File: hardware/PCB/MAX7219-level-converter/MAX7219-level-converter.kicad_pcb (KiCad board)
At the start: 2 copper layers, 21.5 x 10 mm, 4 parts, among them U1 SN74LV1T34DBV, U2 MAX7219, U3 SN74LV1T34DBV, U4 SN74LV1T34DBV

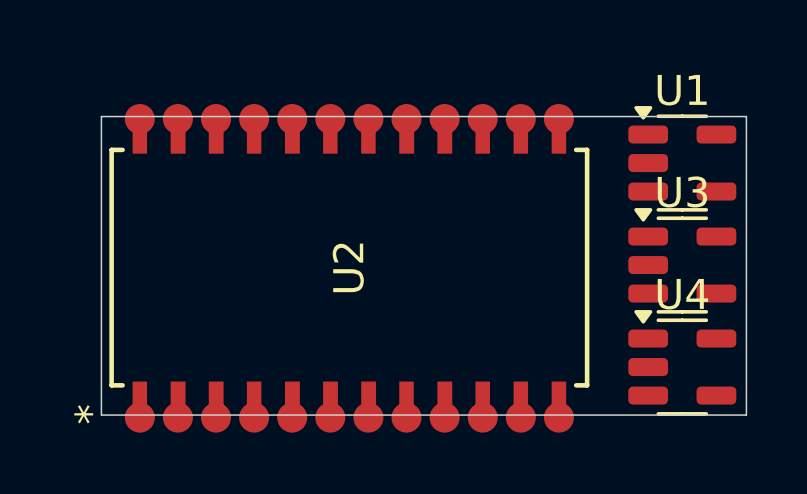
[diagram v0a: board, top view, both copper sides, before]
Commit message: signal level converter for new hardware version 1.0
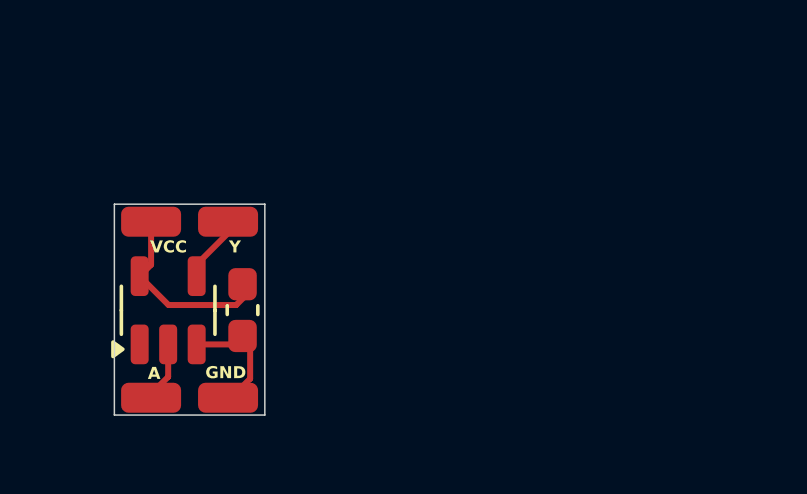
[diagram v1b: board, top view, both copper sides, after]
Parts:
- removed U2: MAX7219, MAX7219:MAX7219-pigipack
- removed U3, U4: SN74LV1T34DBV, Package_TO_SOT_SMD:SOT-23-5
- added C1: 100n/50V, Capacitor_SMD:C_0603_1608Metric_Pad1.08x0.95mm_HandSolder, F.Cu at (140.0, 98.6)
- added J1: VCC, Connector_Wire:SolderWirePad_1x01_SMD_1x2mm, F.Cu at (136.9, 95.6)
- added J2: GND, Connector_Wire:SolderWirePad_1x01_SMD_1x2mm, F.Cu at (139.5, 101.5)
- added J3: Conn_01x01_Pin, Connector_Wire:SolderWirePad_1x01_SMD_1x2mm, F.Cu at (136.9, 101.5)
- added J4: Conn_01x01_Pin, Connector_Wire:SolderWirePad_1x01_SMD_1x2mm, F.Cu at (139.5, 95.6)
- moved U1 17.8 mm to (137.5, 98.6), turned to 90 degrees
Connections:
- U1 pad 2: unconnected-(U1-A-Pad2) -> A
- U1 pad 3: Net-(U1-GND) -> GND
- U1 pad 4: Net-(U1-Y) -> Y
- U1 pad 5: Net-(U1-VCC) -> VCC
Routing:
- net VCC: track 0.00 -> 6.22 mm
- net GND: track 0.00 -> 4.04 mm
- net Y: track 0.00 -> 2.19 mm
- net A: track 0.00 -> 1.89 mm
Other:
- board size 21.5 x 10 mm -> 5 x 7 mm
- board text added: "A"
- board text added: "GND"
- board text added: "VCC"
- board text added: "Y"
